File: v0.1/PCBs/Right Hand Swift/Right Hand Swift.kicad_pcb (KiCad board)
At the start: 2 copper layers, 144.1 x 153 mm, 17 parts, among them J5 FFC Connector

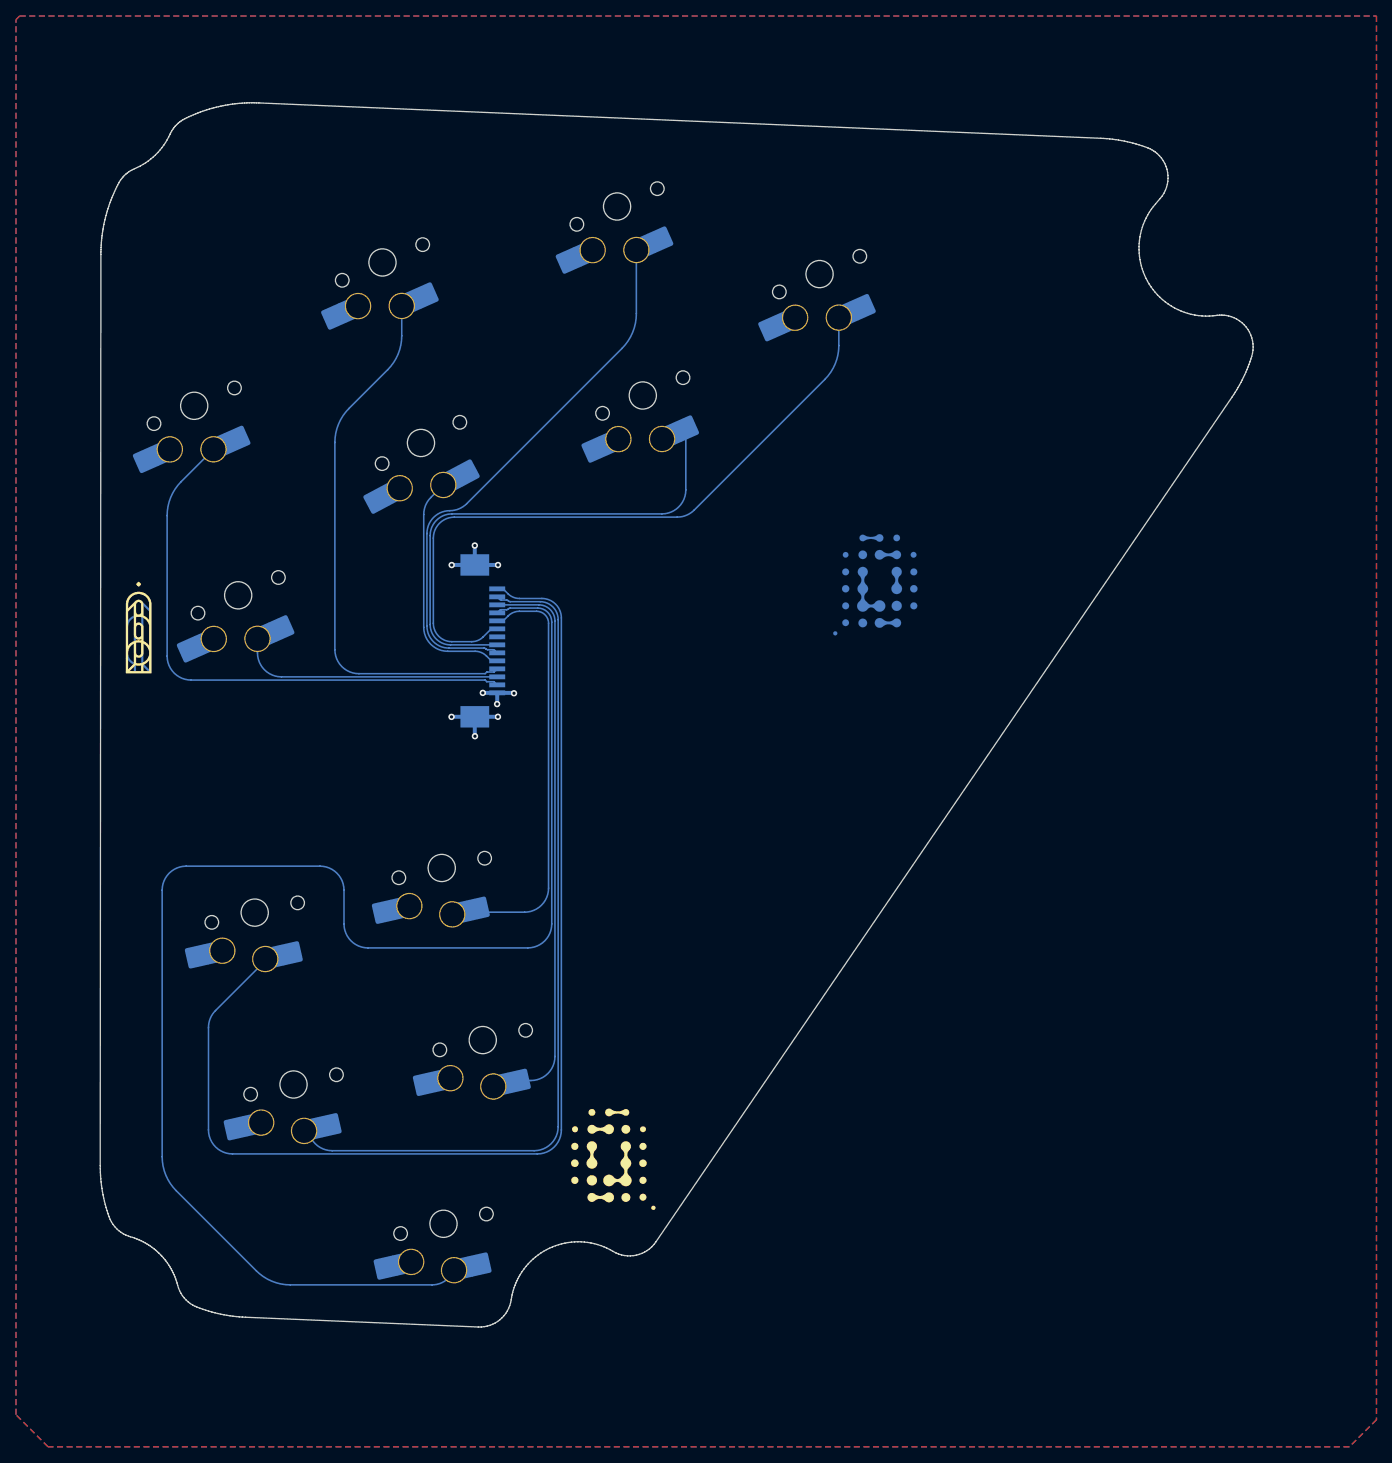
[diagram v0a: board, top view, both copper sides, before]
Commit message: Adjusted Swift right side to the preferred footprint
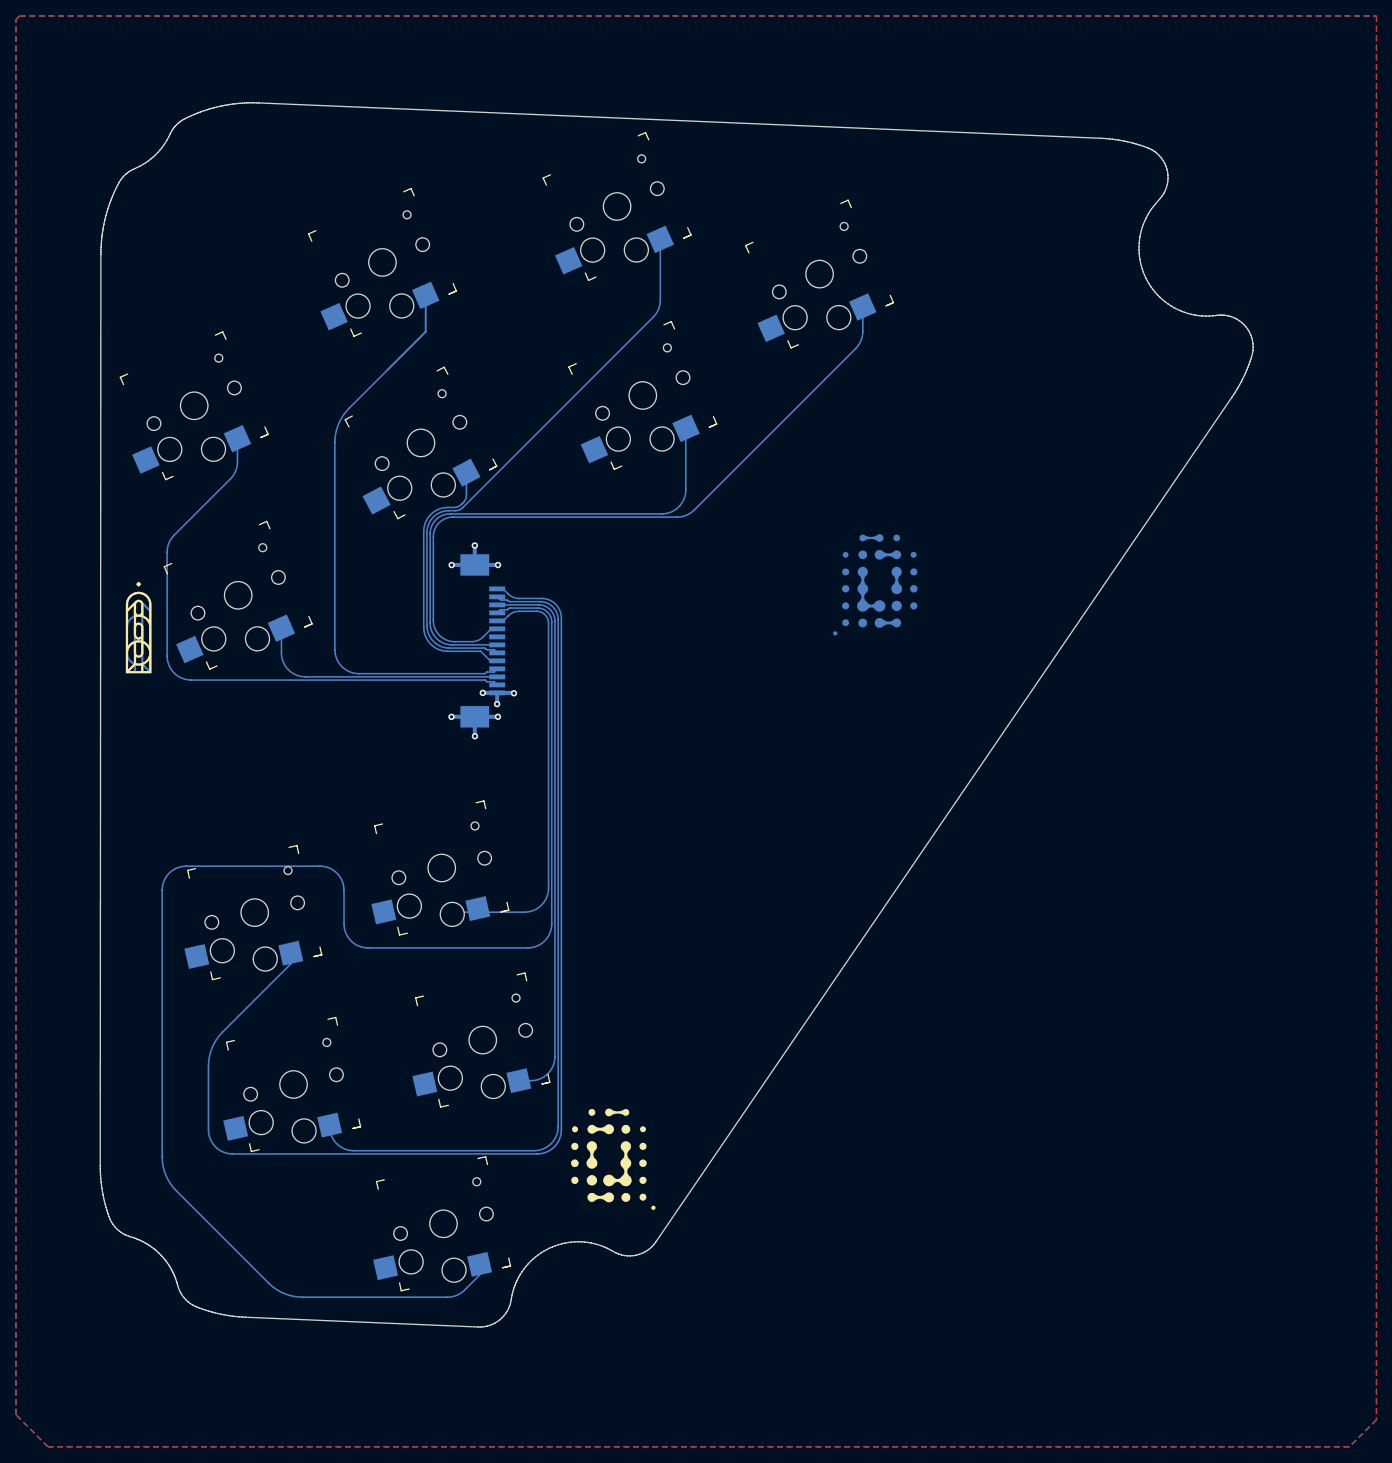
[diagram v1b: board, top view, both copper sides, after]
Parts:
- CH10, CH11, CH12, CH13, CH14, CH15, CH16, CH17, CH18, CH20, CH8, CH9: footprint PCM_marbastlib-choc:SW_choc_v1_HS_1u -> PCBs:Kailh_socket_PG1350; moved to F.Cu
- turned CH10 to 23.9 degrees
- turned CH11 to 23.9 degrees
- turned CH12 to 12.8 degrees
- turned CH13 to 12.8 degrees
- turned CH14 to 28 degrees
- turned CH15 to 12.8 degrees
- turned CH16 to 23.9 degrees
- turned CH17 to 12.8 degrees
- turned CH18 to 23.9 degrees
- turned CH20 to 23.9 degrees
- turned CH8 to 23.9 degrees
- turned CH9 to 12.8 degrees
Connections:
- CH10 pad 1: GND -> Y
- CH10 pad 2: Y -> GND
- CH11 pad 1: GND -> B
- CH11 pad 2: B -> GND
- CH12 pad 1: GND -> C_LT
- CH12 pad 2: C_LT -> GND
- CH13 pad 1: GND -> C_DN
- CH13 pad 2: C_DN -> GND
- CH14 pad 1: GND -> X
- CH14 pad 2: X -> GND
- CH15 pad 1: GND -> C_RT
- CH15 pad 2: C_RT -> GND
- CH16 pad 1: GND -> LS
- CH16 pad 2: LS -> GND
- CH17 pad 1: GND -> A
- CH17 pad 2: A -> GND
- CH18 pad 1: GND -> Z
- CH18 pad 2: Z -> GND
- CH20 pad 1: GND -> UP
- CH20 pad 2: UP -> GND
- CH8 pad 1: GND -> R
- CH8 pad 2: R -> GND
- CH9 pad 1: GND -> C_UP
- CH9 pad 2: C_UP -> GND
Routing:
- net C_DN: track 184.1 -> 188.5 mm
- net X: track 29.8 -> 33.8 mm
- net A: track 72.0 -> 68.9 mm
- net Y: track 68.0 -> 70.8 mm
- net LS: track 68.9 -> 71.8 mm
- net UP: track 85.9 -> 88.5 mm
- net R: track 71.1 -> 73.6 mm
- net C_LT: track 107.1 -> 104.7 mm
- net B: track 33.3 -> 31.6 mm
- net C_UP: track 145.8 -> 147.1 mm

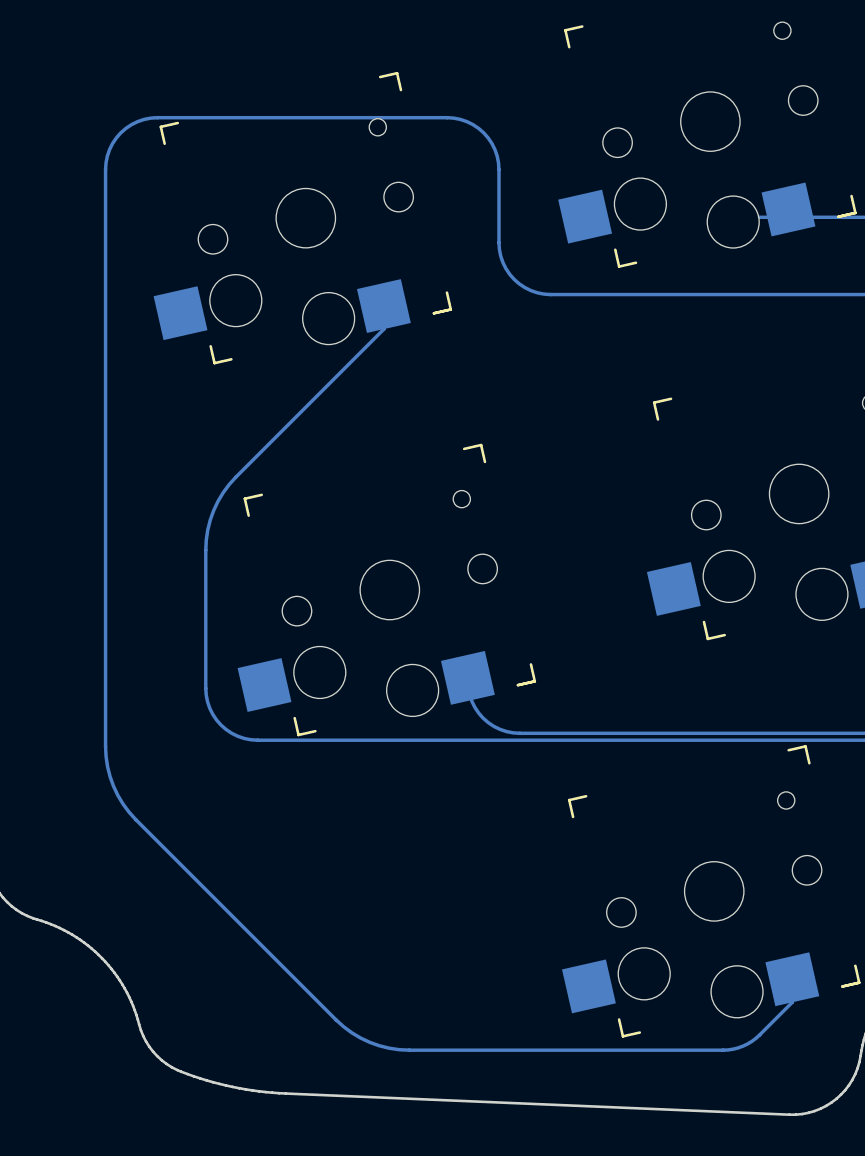
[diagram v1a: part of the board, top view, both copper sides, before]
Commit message: Adjusted daughterboard pinout and drill hole error on right hand
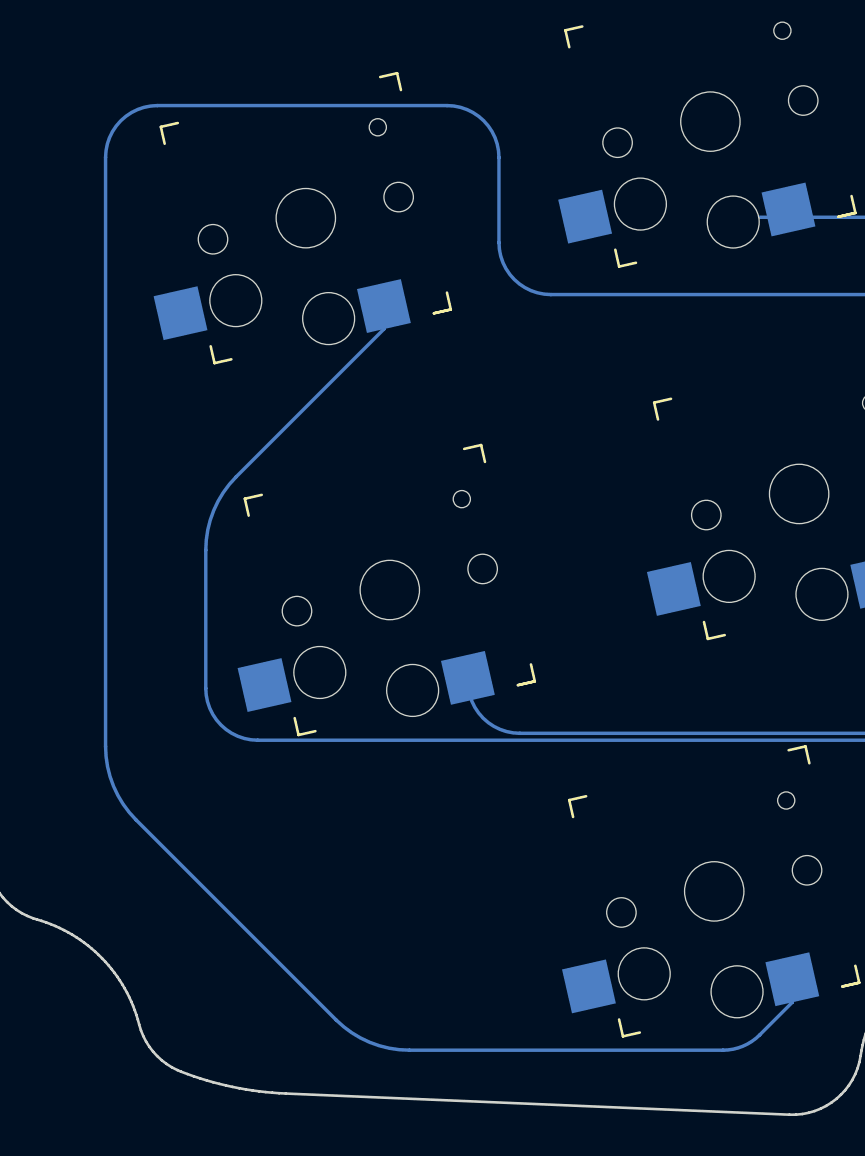
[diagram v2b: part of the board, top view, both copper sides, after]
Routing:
- net C_DN: track 188.5 -> 189.9 mm
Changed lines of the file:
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@@
   (arc (start 82.67 90.422141) (mid 82.080658 88.999342) (end 80.657859 88.41) (width 0.2) (layer "B.Cu") (net 3))
   (arc (start 82.67 144.88636) (mid 81.79132 147.00768) (end 79.67 147.88636) (width 0.2) (layer "B.Cu") (net 3))
+  (segment (start 35.32736 161.63736) (end 46.882641 173.192641) (width 0.2) (layer "B.Cu") (net 4))
+  (segment (start 75.45 89.41) (end 75.757132 89.102868) (width 0.2) (layer "B.Cu") (net 4))
+  (segment (start 75.969264 89.015) (end 76.625736 89.015) (width 0.2) (layer "B.Cu") (net 4))
   (segment (start 71.361972 174.07132) (end 73.24988 172.183412) (width 0.2) (layer "B.Cu") (net 4))
-  (segment (start 35.32736 161.63736) (end 46.882641 173.192641) (width 0.2) (layer "B.Cu") (net 4))
-  (segment (start 53.3 121.07) (end 36.57 121.07) (width 0.2) (layer "B.Cu") (net 4))
-  (segment (start 79.27 131.29) (end 59.3 131.29) (width 0.2) (layer "B.Cu") (net 4))
-  (segment (start 56.3 128.29) (end 56.3 124.07) (width 0.2) (layer "B.Cu") (net 4))
-  (segment (start 76.837868 88.927132) (end 76.867132 88.897868) (width 0.2) (layer "B.Cu") (net 4))
   (segment (start 77.079264 88.81) (end 80.513212 88.81) (width 0.2) (layer "B.Cu") (net 4))
-  (segment (start 75.45 89.41) (end 75.757132 89.102868) (width 0.2) (layer "B.Cu") (net 4))
-  (segment (start 51.125281 174.95) (end 69.240651 174.95) (width 0.2) (layer "B.Cu") (net 4))
   (segment (start 73.24988 172.183412) (end 73.24988 170.850283) (width 0.2) (layer "B.Cu") (net 4))
   (segment (start 82.27 90.566788) (end 82.27 128.29) (width 0.2) (layer "B.Cu") (net 4))
-  (segment (start 33.57 124.07) (end 33.57 157.394719) (width 0.2) (layer "B.Cu") (net 4))
-  (segment (start 75.969264 89.015) (end 76.625736 89.015) (width 0.2) (layer "B.Cu") (net 4))
+  (segment (start 33.57 123.37) (end 33.57 157.394719) (width 0.2) (layer "B.Cu") (net 4))
+  (segment (start 51.125281 174.95) (end 69.240651 174.95) (width 0.2) (layer "B.Cu") (net 4))
+  (segment (start 76.837868 88.927132) (end 76.867132 88.897868) (width 0.2) (layer "B.Cu") (net 4))
+  (segment (start 53.3 120.37) (end 36.57 120.37) (width 0.2) (layer "B.Cu") (net 4))
+  (segment (start 79.27 131.29) (end 59.3 131.29) (width 0.2) (layer "B.Cu") (net 4))
+  (segment (start 56.3 128.29) (end 56.3 123.37) (width 0.2) (layer "B.Cu") (net 4))
   (arc (start 59.3 131.29) (mid 57.17868 130.41132) (end 56.3 128.29) (width 0.2) (layer "B.Cu") (net 4))
-  (arc (start 36.57 121.07) (mid 34.44868 121.94868) (end 33.57 124.07) (width 0.2) (layer "B.Cu") (net 4))
+  (arc (start 82.27 128.29) (mid 81.39132 130.41132) (end 79.27 131.29) (width 0.2) (layer "B.Cu") (net 4))
   (arc (start 80.513212 88.81) (mid 81.755449 89.324551) (end 82.27 90.566788) (width 0.2) (layer "B.Cu") (net 4))
+  (arc (start 33.57 157.394719) (mid 34.026723 159.69082) (end 35.32736 161.63736) (width 0.2) (layer "B.Cu") (net 4))
+  (arc (start 33.57 123.37) (mid 34.44868 121.24868) (end 36.57 120.37) (width 0.2) (layer "B.Cu") (net 4))
+  (arc (start 46.882641 173.192641) (mid 48.829181 174.493277) (end 51.125281 174.95) (width 0.2) (layer "B.Cu") (net 4))
+  (arc (start 56.3 123.37) (mid 55.42132 121.24868) (end 53.3 120.37) (width 0.2) (layer "B.Cu") (net 4))
   (arc (start 76.867132 88.897868) (mid 76.964459 88.832836) (end 77.079264 88.81) (width 0.2) (layer "B.Cu") (net 4))
-  (arc (start 56.3 124.07) (mid 55.42132 121.94868) (end 53.3 121.07) (width 0.2) (layer "B.Cu") (net 4))
-  (arc (start 46.882641 173.192641) (mid 48.829181 174.493277) (end 51.125281 174.95) (width 0.2) (layer "B.Cu") (net 4))
+  (arc (start 69.240651 174.95) (mid 70.388702 174.721639) (end 71.361972 174.07132) (width 0.2) (layer "B.Cu") (net 4))
+  (arc (start 75.757132 89.102868) (mid 75.854459 89.037836) (end 75.969264 89.015) (width 0.2) (layer "B.Cu") (net 4))
   (arc (start 76.625736 89.015) (mid 76.740541 88.992164) (end 76.837868 88.927132) (width 0.2) (layer "B.Cu") (net 4))
-  (arc (start 71.361972 174.07132) (mid 70.388702 174.721639) (end 69.240651 174.95) (width 0.2) (layer "B.Cu") (net 4))
-  (arc (start 33.57 157.394719) (mid 34.026723 159.69082) (end 35.32736 161.63736) (width 0.2) (layer "B.Cu") (net 4))
-  (arc (start 82.27 128.29) (mid 81.39132 130.41132) (end 79.27 131.29) (width 0.2) (layer "B.Cu") (net 4))
-  (arc (start 75.757132 89.102868) (mid 75.854459 89.037836) (end 75.969264 89.015) (width 0.2) (layer "B.Cu") (net 4))
   (segment (start 81.87 90.71) (end 81.87 123.823413) (width 0.2) (layer "B.Cu") (net 5))
   (segment (start 75.45 90.41) (end 76.2 90.41) (width 0.2) (layer "B.Cu") (net 5))
